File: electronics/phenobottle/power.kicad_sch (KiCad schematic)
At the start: 14 parts

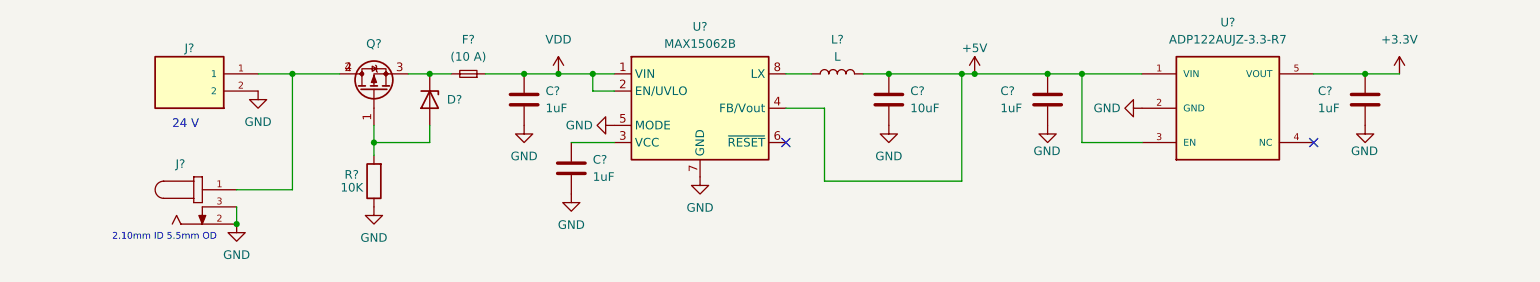
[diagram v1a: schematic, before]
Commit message: updated 5V LDO with something that can power a RPi zero and other peripherals
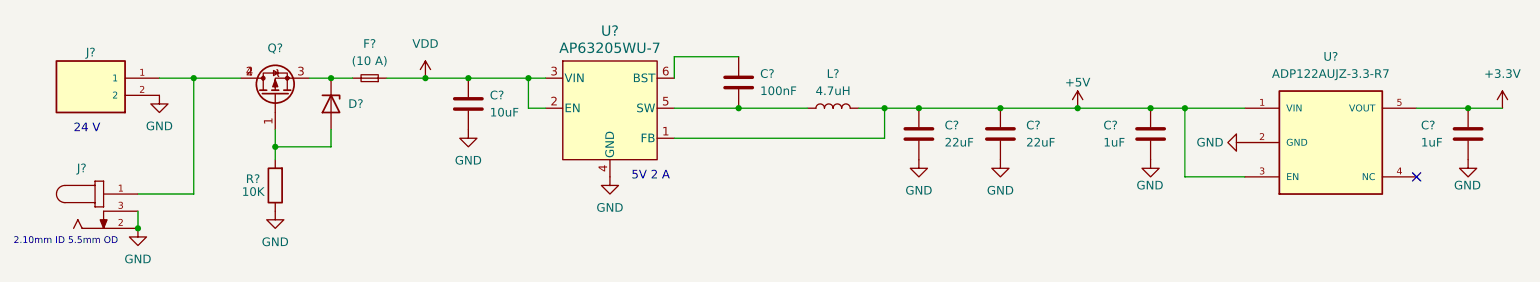
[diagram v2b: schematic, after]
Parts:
- removed C? (x2): 1uF, Capacitor_SMD:C_0805_2012Metric, symbol Device:C
- removed C?: 10uF, Capacitor_SMD:C_0805_2012Metric, symbol Device:C
- removed L?: L, inductors:VLS6045EX-470M, symbol Device:L
- removed U?: MAX15062B, Package_DFN_QFN:DFN-8_2x2mm_P0.5mm, symbol Regulator_Switching:MAX15062B
- added C? (x2): 22uF, Capacitor_SMD:C_0805_2012Metric, symbol Device:C
- added C?: 100nF, Capacitor_SMD:C_0805_2012Metric, symbol Device:C
- added C?: 10uF, Capacitor_SMD:C_0805_2012Metric, symbol Device:C
- added L?: 4.7uH, Inductor_SMD:L_Bourns_SRN8040TA, symbol Device:L
- added U?: AP63205WU-7, ldo:AP63205WU-7, symbol ldo:AP63205WU-7
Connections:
- net +5V: now also C?.1, C?.1, L?.2, U?.1 (FB)
- net GND: now also C?.2, C?.2, C?.2, U?.4 (GND)
- net VDD: now also C?.1, U?.2 (EN), U?.3 (VIN)
- new net: C?.1, U?.6 (BST)
- new net: C?.2, L?.1, U?.5 (SW)
- no-connect marks 2 -> 1
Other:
- note added: "5V 2 A"
- moved on the sheet: C?, D?, F?, J?, Q?, R?, U?
